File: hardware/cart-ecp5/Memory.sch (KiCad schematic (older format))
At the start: 12 parts, among them J2 MicroSD_Molex_1040310811, U3 S27KS0641

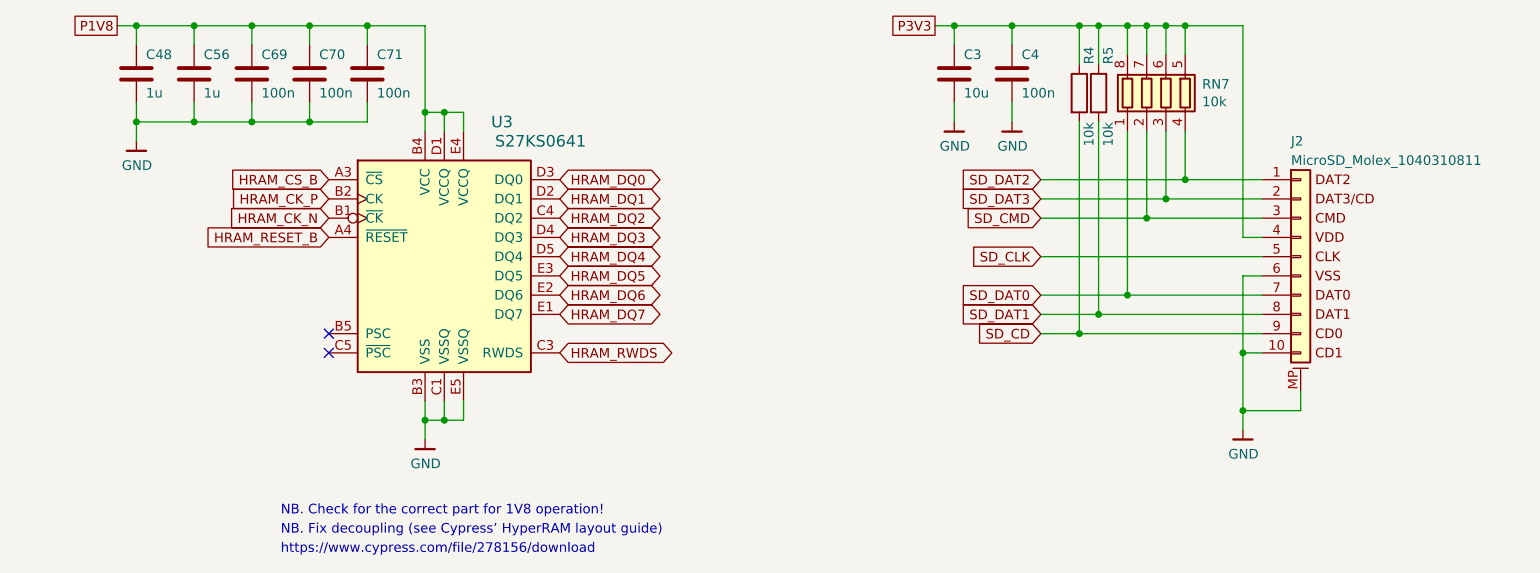
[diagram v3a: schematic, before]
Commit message: Assign MPN for hyperram device
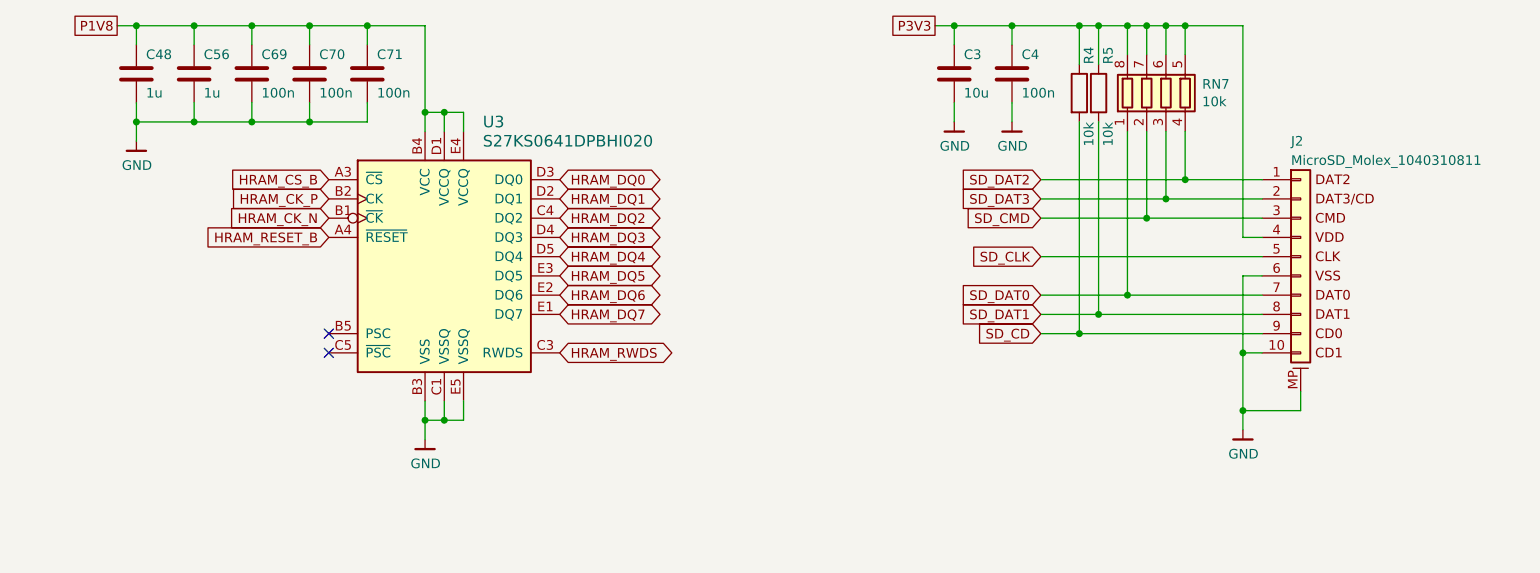
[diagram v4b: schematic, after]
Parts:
- U3: value S27KS0641 -> S27KS0641DPBHI020; MPN S27KS0641 -> S27KS0641DPBHI020
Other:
- note removed: "NB. Check for the correct part for 1V8 operation!"
- note removed: "NB. Fix decoupling (see Cypress’ HyperRAM layout guide)"
- note removed: "https://www.cypress.com/file/278156/download"
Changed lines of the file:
@@
 U 1 1 5F47DAAE
 P 4250 4100
-F 0 "U3" H 4550 4900 60  0000 C CNN
-F 1 "S27KS0641" H 4750 4800 60  0000 C CNN
+F 0 "U3" H 4450 4900 60  0000 L CNN
+F 1 "S27KS0641DPBHI020" H 4450 4800 60  0000 L CNN
 F 2 "ng_package_bga:BGA-24_6.0x8.0mm_Layout5x5_P1.0mm_Pad0.4mm" H 3450 6050 60  0001 C CNN
 F 3 "https://www.cypress.com/file/183506/download" H 3450 6050 60  0001 C CNN
 F 4 "Cypress" H 4250 4100 50  0001 C CNN "MFR"
-F 5 "S27KS0641" H 4250 4100 50  0001 C CNN "MPN"
+F 5 "S27KS0641DPBHI020" H 4250 4100 50  0001 C CNN "MPN"
 	1    4250 4100
 	1    0    0    -1
@@
 Wire Wire Line
 	8100 3600 8500 3600
-Text Notes 3400 5350 0    50   ~ 0
-NB. Check for the correct part for 1V8 operation!
 $Comp
 L Device:C C71
@@
 	1    0    0    -1
 $EndComp
-Text Notes 3400 5450 0    50   ~ 0
-NB. Fix decoupling (see Cypress’ HyperRAM layout guide)
-Text Notes 3400 5550 0    50   ~ 0
-https://www.cypress.com/file/278156/download
 $Comp
 L Device:C C56

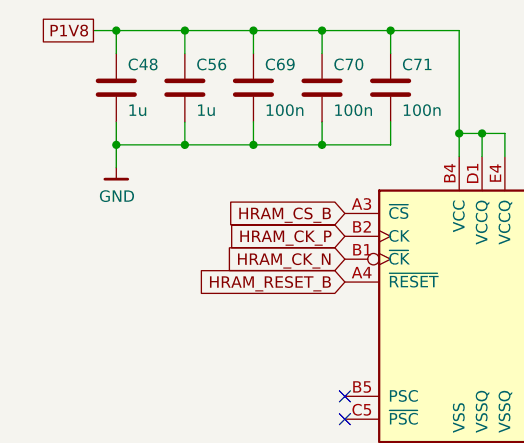
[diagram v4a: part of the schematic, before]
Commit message: Add ground test point for hyperram interface
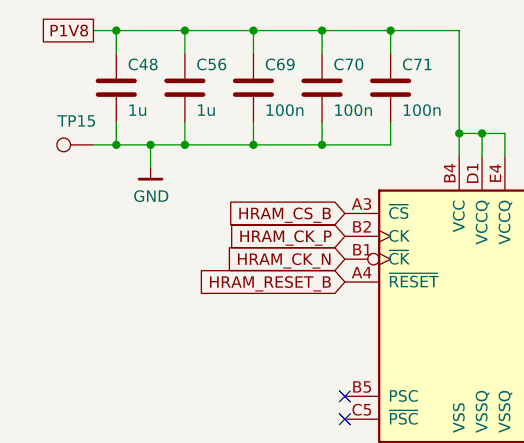
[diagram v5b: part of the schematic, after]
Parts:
- added TP15: TestPoint, TestPoint:TestPoint_Pad_D1.0mm, symbol Connector:TestPoint
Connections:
- net GND: now also TP15.1
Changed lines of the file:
@@
 L ng_power:GND #PWR068
 U 1 1 5F5F4633
-P 2650 3400
-F 0 "#PWR068" H 2650 3150 50  0001 C CNN
-F 1 "GND" H 2653 3274 50  0000 C CNN
-F 2 "" H 2550 3050 50  0001 C CNN
-F 3 "" H 2650 3400 50  0001 C CNN
-	1    2650 3400
+P 2800 3400
+F 0 "#PWR068" H 2800 3150 50  0001 C CNN
+F 1 "GND" H 2803 3274 50  0000 C CNN
+F 2 "" H 2700 3050 50  0001 C CNN
+F 3 "" H 2800 3400 50  0001 C CNN
+	1    2800 3400
 	1    0    0    -1
 $EndComp
@@
 	2650 3200 2650 3300
 Wire Wire Line
-	2650 3300 2950 3300
+	2650 3300 2800 3300
 Connection ~ 2650 3300
 Wire Wire Line
-	2650 3300 2650 3400
+	2800 3300 2800 3400
 Wire Wire Line
 	2950 3300 3250 3300
@@
 	3850 2800 4150 2800
 Connection ~ 3850 2800
+$Comp
+L Connector:TestPoint TP15
+U 1 1 601920AB
+P 2550 3300
+F 0 "TP15" V 2653 3372 50  0000 C CNN
+F 1 "TestPoint" V 2654 3372 50  0001 C CNN
+F 2 "TestPoint:TestPoint_Pad_D1.0mm" H 2750 3300 50  0001 C CNN
+F 3 "~" H 2750 3300 50  0001 C CNN
+	1    2550 3300
+	0    -1   -1   0
+$EndComp
+Wire Wire Line
+	2550 3300 2650 3300
+Connection ~ 2800 3300
+Wire Wire Line
+	2800 3300 2950 3300
 $EndSCHEMATC
